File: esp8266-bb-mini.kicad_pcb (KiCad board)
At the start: 2 copper layers, 34.3 x 31.8 mm, 18 parts, among them J1 Conn_01x02_Male, J2 Conn_01x04_Male, J3 Conn_01x04_Male, J4 Conn_01x04_Male, J5 Conn_01x04_Male, U1 LP38693MP-3.3, U2 ESP-12F

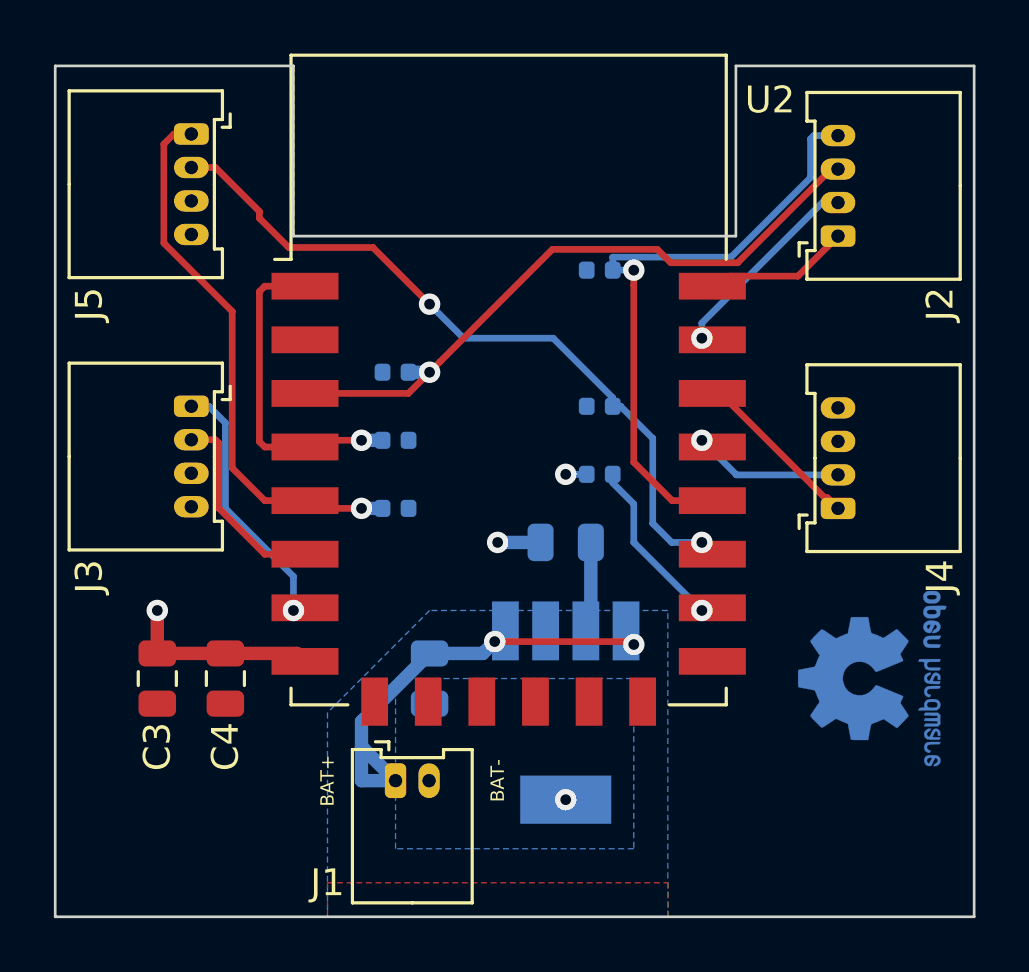
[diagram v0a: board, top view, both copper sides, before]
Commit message: update layout
- add mounting holes; in order to place them diagonally move the connectors around a little
- add informative texts

Signed-off-by: Tillmann Heidsieck <theidsieck@leenox.de>
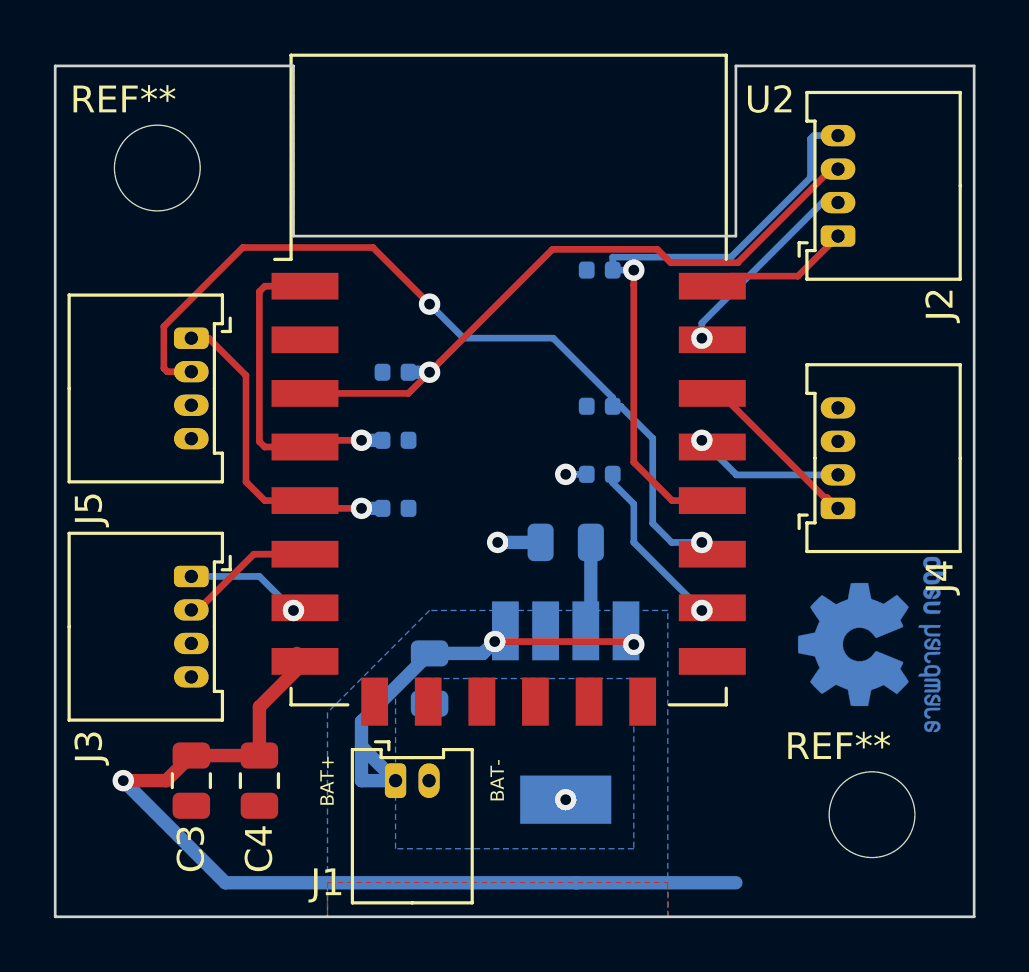
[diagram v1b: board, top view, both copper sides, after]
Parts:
- added REF**: MountingHole_3.2mm_M3, MountingHole:MountingHole_3.2mm_M3, F.Cu at (147.3, 114.3)
- added REF**: MountingHole_3.2mm_M3, MountingHole:MountingHole_3.2mm_M3, F.Cu at (120.7, 90.2)
- moved J5 7.62 mm to (121.9, 96.5)
- moved J3 6.35 mm to (121.9, 105.4)
- moved C3 4.02 mm to (121.9, 113.0)
- moved C4 4.02 mm to (124.5, 113.0)
- moved REF** 1.27 mm to (147.3, 108.0)
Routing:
- net +3V3: track 10.8 -> 38.1 mm
- net /EXT_GPIO14: track 20.6 -> 12.1 mm
- net /EXT_GPIO13: track 9.58 -> 4.34 mm
- net /EXT_GPIO2: track 27.0 -> 30.5 mm
- net /EXT_GPIO12: track 7.43 -> 4.88 mm
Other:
- board text added: "ESP8266 Mini Breakout-Board v1.0"
- board text added: "Source under https://bit.ly/39piDbX"
